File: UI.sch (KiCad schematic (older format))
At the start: 7 parts, among them SW501 SEL

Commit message: current
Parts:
- added C503, C504: 100n, Capacitor_SMD:C_0603_1608Metric, symbol Device:C
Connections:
- net ENC_A: now also C504.2
- net ENC_B: now also C503.2
- net GND: now also C503.1, C504.1
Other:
- note removed: "Better with additional de-bounce caps 100nF, retro fit 2 of them between A+C and B+C."
- moved on the sheet: R501, R502
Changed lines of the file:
@@
 Title "ESP32 Eurorack Audio Module"
 Date "2019-03-27"
-Rev "B2-public"
+Rev "C"
 Comp "(c) Robert Manzke 2019"
 Comment1 "https://creativecommons.org/licenses/by-nc-sa/4.0/"
@@
 L Device:R R502
 U 1 1 5B68F96E
-P 3100 4400
-F 0 "R502" H 3170 4446 50  0000 L CNN
-F 1 "10k" H 3170 4355 50  0000 L CNN
-F 2 "Resistor_SMD:R_0603_1608Metric" V 3030 4400 50  0001 C CNN
-F 3 "~" H 3100 4400 50  0001 C CNN
-	1    3100 4400
-	1    0    0    -1
-$EndComp
-Wire Wire Line
-	3400 4700 3100 4700
-Wire Wire Line
-	3100 4700 3100 4550
+P 2550 4400
+F 0 "R502" H 2620 4446 50  0000 L CNN
+F 1 "10k" H 2620 4355 50  0000 L CNN
+F 2 "Resistor_SMD:R_0603_1608Metric" V 2480 4400 50  0001 C CNN
+F 3 "~" H 2550 4400 50  0001 C CNN
+	1    2550 4400
+	1    0    0    -1
+$EndComp
+Wire Wire Line
+	3400 4700 2550 4700
+Wire Wire Line
+	2550 4700 2550 4550
 $Comp
 L Device:R R501
 U 1 1 5B68FC31
-P 2800 4400
-F 0 "R501" H 2870 4446 50  0000 L CNN
-F 1 "10k" H 2870 4355 50  0000 L CNN
-F 2 "Resistor_SMD:R_0603_1608Metric" V 2730 4400 50  0001 C CNN
-F 3 "~" H 2800 4400 50  0001 C CNN
-	1    2800 4400
-	1    0    0    -1
-$EndComp
-Wire Wire Line
-	3400 4900 2800 4900
-Wire Wire Line
-	2800 4900 2800 4550
+P 2150 4400
+F 0 "R501" H 2220 4446 50  0000 L CNN
+F 1 "10k" H 2220 4355 50  0000 L CNN
+F 2 "Resistor_SMD:R_0603_1608Metric" V 2080 4400 50  0001 C CNN
+F 3 "~" H 2150 4400 50  0001 C CNN
+	1    2150 4400
+	1    0    0    -1
+$EndComp
+Wire Wire Line
+	3400 4900 2150 4900
+Wire Wire Line
+	2150 4900 2150 4550
 $Comp
 L Device:R R503
@@
 L power:+3V3 #PWR0504
 U 1 1 5B6902D6
-P 2800 4100
-F 0 "#PWR0504" H 2800 3950 50  0001 C CNN
-F 1 "+3V3" H 2815 4273 50  0000 C CNN
-F 2 "" H 2800 4100 50  0001 C CNN
-F 3 "" H 2800 4100 50  0001 C CNN
-	1    2800 4100
-	1    0    0    -1
-$EndComp
-Wire Wire Line
-	2800 4100 2800 4150
+P 2150 4100
+F 0 "#PWR0504" H 2150 3950 50  0001 C CNN
+F 1 "+3V3" H 2165 4273 50  0000 C CNN
+F 2 "" H 2150 4100 50  0001 C CNN
+F 3 "" H 2150 4100 50  0001 C CNN
+	1    2150 4100
+	1    0    0    -1
+$EndComp
+Wire Wire Line
+	2150 4100 2150 4150
 Wire Wire Line
 	4200 4250 4200 4150
 Wire Wire Line
-	4200 4150 3100 4150
-Connection ~ 2800 4150
-Wire Wire Line
-	2800 4150 2800 4250
-Wire Wire Line
-	3100 4250 3100 4150
-Connection ~ 3100 4150
-Wire Wire Line
-	3100 4150 2800 4150
+	4200 4150 2550 4150
+Connection ~ 2150 4150
+Wire Wire Line
+	2150 4150 2150 4250
+Wire Wire Line
+	2550 4250 2550 4150
+Connection ~ 2550 4150
+Wire Wire Line
+	2550 4150 2150 4150
 Text HLabel 4850 4700 2    50   Output ~ 0
 ENC_BTN
@@
 Connection ~ 4200 4700
 Wire Wire Line
-	2800 4900 2400 4900
-Connection ~ 2800 4900
-Wire Wire Line
-	3100 4700 2400 4700
-Connection ~ 3100 4700
-Text HLabel 2400 4700 0    50   Output ~ 0
+	2150 4900 1750 4900
+Connection ~ 2150 4900
+Connection ~ 2550 4700
+Text HLabel 1750 4700 0    50   Output ~ 0
 ENC_A
-Text HLabel 2400 4900 0    50   Output ~ 0
+Text HLabel 1750 4900 0    50   Output ~ 0
 ENC_B
 Text Label 3800 2700 0    50   ~ 0
@@
 Text Label 3800 3100 0    50   ~ 0
 SCK
-Text Label 2500 4700 0    50   ~ 0
+Text Label 1850 4700 0    50   ~ 0
 ENC_A
-Text Label 2500 4900 0    50   ~ 0
+Text Label 1850 4900 0    50   ~ 0
 ENC_B
 Text Label 4400 4700 0    50   ~ 0
@@
 Text Notes 2500 3350 1    50   ~ 0
 MDF7-9S-2.54DSA(55) and\nMDF7-5S-2.54DSA(55)
-Text Notes 1950 5400 0    50   ~ 0
-Better with additional de-bounce caps 100nF, retro fit 2 of them between A+C and B+C.
+$Comp
+L Device:C C504
+U 1 1 5CA39CAD
+P 2550 5200
+F 0 "C504" H 2435 5154 50  0000 R CNN
+F 1 "100n" H 2435 5245 50  0000 R CNN
+F 2 "Capacitor_SMD:C_0603_1608Metric" H 2588 5050 50  0001 C CNN
+F 3 "~" H 2550 5200 50  0001 C CNN
+	1    2550 5200
+	-1   0    0    1
+$EndComp
+Wire Wire Line
+	2550 4700 2550 5050
+$Comp
+L Device:C C503
+U 1 1 5CA3E66E
+P 2150 5200
+F 0 "C503" H 2035 5154 50  0000 R CNN
+F 1 "100n" H 2035 5245 50  0000 R CNN
+F 2 "Capacitor_SMD:C_0603_1608Metric" H 2188 5050 50  0001 C CNN
+F 3 "~" H 2150 5200 50  0001 C CNN
+	1    2150 5200
+	-1   0    0    1
+$EndComp
+Wire Wire Line
+	2150 4900 2150 5050
+$Comp
+L power:GND #PWR0502
+U 1 1 5CA3F1C4
+P 2550 5500
+F 0 "#PWR0502" H 2550 5250 50  0001 C CNN
+F 1 "GND" H 2555 5327 50  0000 C CNN
+F 2 "" H 2550 5500 50  0001 C CNN
+F 3 "" H 2550 5500 50  0001 C CNN
+	1    2550 5500
+	1    0    0    -1
+$EndComp
+Wire Wire Line
+	2150 5350 2150 5450
+Wire Wire Line
+	2150 5450 2550 5450
+Wire Wire Line
+	2550 5450 2550 5500
+Wire Wire Line
+	2550 5350 2550 5450
+Connection ~ 2550 5450
+Wire Wire Line
+	1750 4700 2550 4700
 $EndSCHEMATC

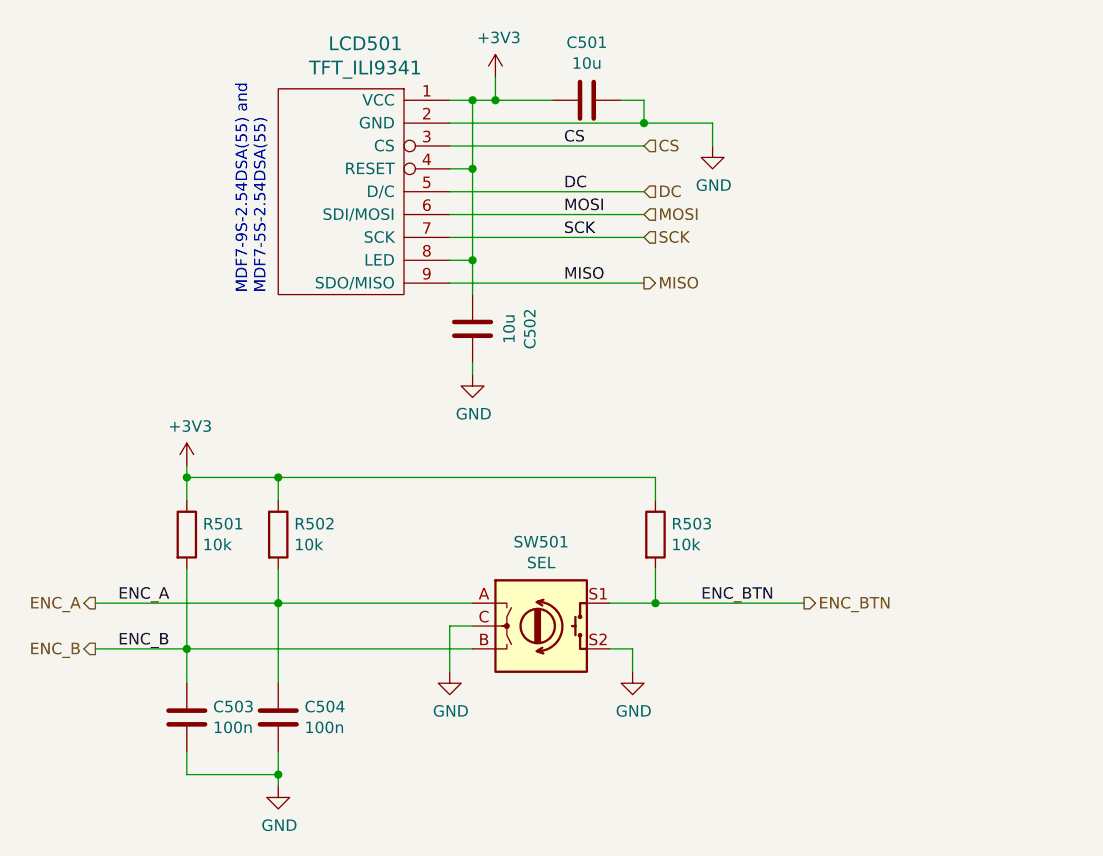
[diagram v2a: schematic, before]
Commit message: cleaned up schematic
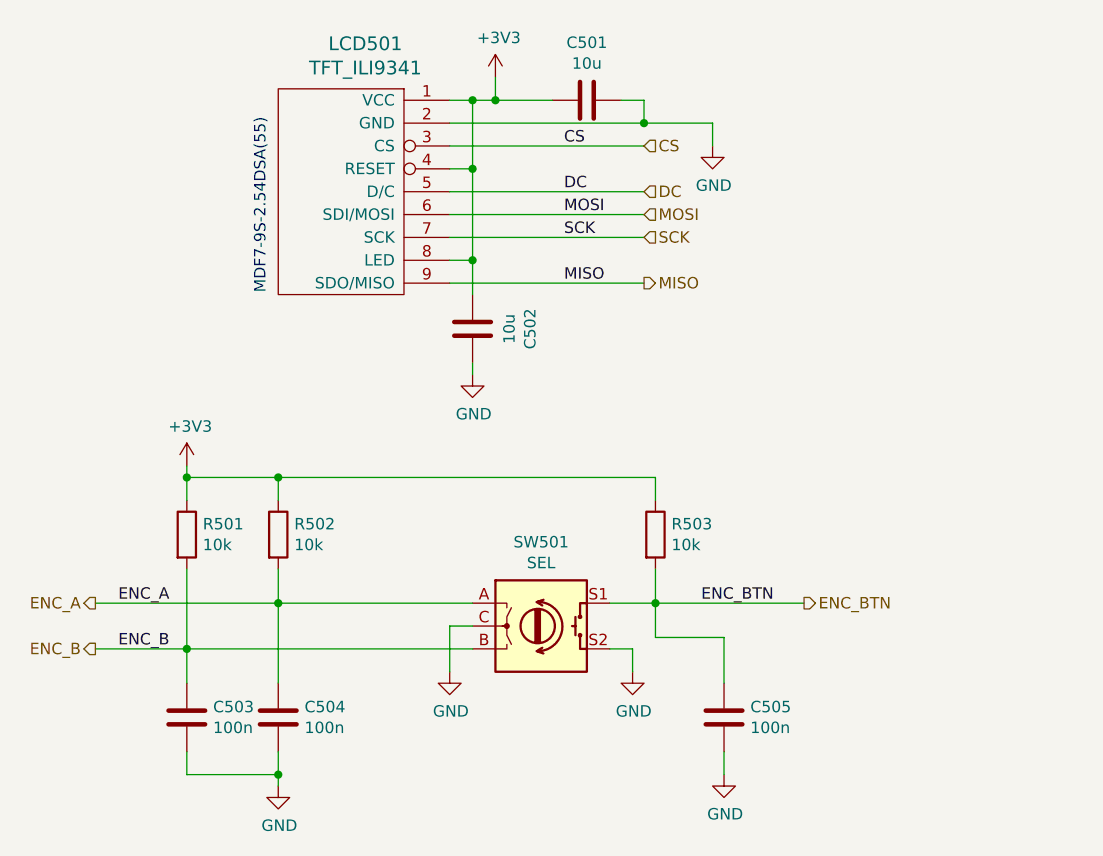
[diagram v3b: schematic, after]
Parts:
- added C505: 100n, Capacitor_SMD:C_0603_1608Metric, symbol Device:C
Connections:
- net ENC_BTN: now also C505.2
- net GND: now also C505.1
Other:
- note added: "MDF7-9S-2.54DSA(55)"
- note removed: "MDF7-9S-2.54DSA(55) and\nMDF7-5S-2.54DSA(55)"
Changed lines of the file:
@@
 Sheet 5 8
 Title "ESP32 Eurorack Audio Module"
-Date "2019-03-27"
-Rev "C"
+Date "2019-05-13"
+Rev "D"
 Comp "(c) Robert Manzke 2019"
 Comment1 "https://creativecommons.org/licenses/by-nc-sa/4.0/"
@@
 	3400 3650 3400 3700
 Text Notes 2500 3350 1    50   ~ 0
-MDF7-9S-2.54DSA(55) and\nMDF7-5S-2.54DSA(55)
+MDF7-9S-2.54DSA(55)
 $Comp
 L Device:C C504
@@
 Wire Wire Line
 	1750 4700 2550 4700
+$Comp
+L Device:C C505
+U 1 1 5CDB2DC9
+P 4500 5200
+F 0 "C505" H 4385 5154 50  0000 R CNN
+F 1 "100n" H 4385 5245 50  0000 R CNN
+F 2 "Capacitor_SMD:C_0603_1608Metric" H 4538 5050 50  0001 C CNN
+F 3 "~" H 4500 5200 50  0001 C CNN
+	1    4500 5200
+	-1   0    0    1
+$EndComp
+$Comp
+L power:GND #PWR0111
+U 1 1 5CDB35D2
+P 4500 5450
+F 0 "#PWR0111" H 4500 5200 50  0001 C CNN
+F 1 "GND" H 4505 5277 50  0000 C CNN
+F 2 "" H 4500 5450 50  0001 C CNN
+F 3 "" H 4500 5450 50  0001 C CNN
+	1    4500 5450
+	1    0    0    -1
+$EndComp
+Wire Wire Line
+	4500 5350 4500 5450
+Wire Wire Line
+	4200 4700 4200 4850
+Wire Wire Line
+	4200 4850 4500 4850
+Wire Wire Line
+	4500 4850 4500 5050
 $EndSCHEMATC
